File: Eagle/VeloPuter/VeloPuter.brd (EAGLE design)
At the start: 98.7 x 58.4 mm, 39 parts, among them IC1 LM2931, IC2 B7546, IC3 B7546, Q1 BSS92, Q2 BSS101

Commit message: - Added alternative components for the LDDs to be   placed at the same positions - Added 5V USB - Added overall Power off - Added 6th LDD/switch (was 5) -> possible also for buzzer.   Note that a key for this is NOT available. Possibly the   config or the hazzard button can be freed for this.
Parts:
- removed BLINKERS: (no value), con-phoenix_3.81_mcv:MCV4
- removed H1, H2, H3: MOUNT-HOLE3.6, holes:3,6
- removed IC1: LM2931, v-reg-3-gbeu:TO220L1
- added AUX_OUT: Aux, con-phoenix_3.81_mcv:MCV6
- added DC1: R-78C5.0-1.0, dc-dc-converter:SIP3
- added JP1, JP2, JP3, JP4, JP5, JP6: (no value), jumper:JP1
- added LM2931: 7805TV, linear:TO220V
- added Q10, Q12, Q14, Q4, Q6, Q8: (no value), transistor-power:TO220BV
- added Q11, Q13, Q3, Q5, Q7, Q9: BS170, transistor-small-signal:SOT54E
- added RN1: 100k, resistor-sil:SIL7
- IC2: device transistor-power:TO220BH -> transistor-small-signal:SOT54E
- IC3: device transistor-power:TO220BH -> transistor-power:TO220BV
- LIGHTS: value (none) -> Lights; device con-phoenix_3.81_mcv:MCV6 -> con-phoenix_3.81_mcv:MCV8
- Q1: value BSS92 -> (none); device transistor-fet:TO92 -> transistor-power:TO220BV
- Q2: value BSS101 -> BS170; device transistor-fet:TO92 -> transistor-small-signal:SOT54E
- moved R9 526.3 mm to (-80.0, -455.9), turned to 0 degrees
- moved R10 501.8 mm to (-80.0, -517.5)
- moved Q2 473.9 mm to (-1.27, -530.2)
- moved R4 470.6 mm to (-80.0, -394.3), turned to 0 degrees
- moved R3 403.9 mm to (-80.0, -332.7), turned to 0 degrees
- moved R2 341.0 mm to (-80.0, -271.1), turned to 0 degrees
- moved R1 274.1 mm to (-65.4, -209.6)
- moved LIGHTS 241.0 mm to (-54.6, -142.9), turned to 0 degrees
- turned IC2 to 270 degrees
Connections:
- removed net N$12: LIGHTS.3, U$5.+VOUT
- removed net ONOFF: ARDUINO_MICRO.A5, Q2.2
- new net N$17: Q3.D, Q4.G, R1.1
- new net N$23: Q7.D, Q8.G, R3.1
- new net N$28: Q10.G, Q9.D, R4.1
- new net N$29: AUX_OUT.1, Q12.S, U$5.+VOUT
- new net N$33: Q11.D, Q12.G, R9.1
- new net N$34: AUX_OUT.3, Q14.S, U$1.+VOUT
- new net N$39: AUX_OUT.4, JP6.2, U$1.-VOUT
- new net N$40: Q13.D, Q14.G, R10.1
- new net POWER_ONOFF: ARDUINO_MICRO.A5, Q2.G
- new net V_USB: AUX_OUT.5, DC1.3
- net 5V: now also CAD.3, LM2931.3; no longer CAD.1, IC1.3
- net CAD_SWITCH: now also CAD.1; no longer CAD.3
- net GND: now also AUX_OUT.6, DC1.2, JP1.1, JP2.1, JP3.1, JP4.1, JP5.1, JP6.1, LM2931.2, Q11.S, Q13.S, Q2.S, Q3.S, Q5.S, Q7.S, Q9.S, RN1.1; no longer IC1.2, Q2.1, R1.1, R10.1, R2.1, R3.1, R4.1, R9.1
- net N$10: now also Q4.S
- net N$11: now also JP1.2
- net N$13: now also AUX_OUT.2, JP5.2; no longer LIGHTS.4
- net N$15: now also Q1.G, Q2.D; no longer Q1.1, Q2.3
- net N$20: now also Q5.D, Q6.G, R2.1; no longer BRAKE.+VIN
- net N$3: now also LIGHTS.3, Q6.S; no longer LIGHTS.5
- net N$5: now also JP2.2, LIGHTS.4; no longer LIGHTS.6
- net N$6: now also LIGHTS.5, Q8.S; no longer BLINKERS.1
- net N$7: now also JP3.2, LIGHTS.6; no longer BLINKERS.2
- net N$8: now also LIGHTS.7, Q10.S; no longer BLINKERS.3
- net N$9: now also JP4.2, LIGHTS.8; no longer BLINKERS.4
- net ONOFF_AUX2: now also Q13.G, RN1.2; no longer R10.2
- net PWM_AUX1: now also Q11.G, RN1.3; no longer R9.2
- net PWM_FRONT: now also Q3.G, RN1.5; no longer R4.2
- net PWM_LEFT: now also Q7.G, RN1.7; no longer R2.2
- net PWM_REAR: now also Q5.G, RN1.4; no longer R1.2
- net PWM_RIGHT: now also Q9.G, RN1.6; no longer R3.2
- net V+: now also LM2931.1, Q1.D; no longer IC1.1, Q1.2
- net VDD: now also BRAKE.+VIN, DC1.1, Q1.S, Q10.D, Q12.D, Q14.D, Q4.D, Q6.D, Q8.D, R1.2, R10.2, R2.2, R3.2, R4.2, R9.2; no longer Q1.3
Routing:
- net PWM_RIGHT: track 102.8 -> 0.00 mm, vias 2 -> 0
- net 5V: track 93.7 -> 0.00 mm
- net PWM_LEFT: track 89.8 -> 0.00 mm
- net PWM_REAR: track 83.5 -> 0.00 mm
- net V+: track 72.2 -> 0.00 mm
- net PWM_FRONT: track 69.9 -> 0.00 mm
- net PWM_AUX1: track 67.4 -> 0.00 mm
- net N$14: track 66.7 -> 0.00 mm
- net SDA_OLED: track 51.9 -> 0.00 mm
- net V_0: track 50.7 -> 0.00 mm
- net SCL_OLED: track 48.4 -> 0.00 mm
- net CONFIG_SWITCH: track 46.8 -> 0.00 mm
- net ALARM_SWITCH: track 37.4 -> 0.00 mm
- net CAD_SWITCH: track 36.6 -> 0.00 mm
- net PWM_BUZZER: track 35.7 -> 0.00 mm
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- removed copper zone on layer 1, net GND
- removed copper zone on layer 16, net GND
- removed copper zone on layer 1, net V+
- removed copper zone on layer 1, net V-
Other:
- board size 98.7 x 58.4 mm -> 100 x 59.7 mm

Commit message: Finished placing the components. Next: routing the connections.
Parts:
- Q1, Q10, Q12, Q14, Q4, Q6, Q8: value (none) -> 4P04L04
- R7: value 3M -> 300k
- R8: value 1M -> 100k
- moved Q3 640.8 mm to (6.99, 34.3)
- moved Q5 628.3 mm to (18.4, 34.3)
- moved Q7 616.1 mm to (29.8, 34.3)
- moved Q9 604.1 mm to (41.3, 34.3)
- moved Q11 592.4 mm to (52.7, 34.3)
- moved Q13 580.9 mm to (64.1, 34.3)
- moved R10 570.3 mm to (59.1, 35.6), turned to 270 degrees
- moved Q14 549.6 mm to (60.3, 45.7), turned to 90 degrees
- moved JP6 539.9 mm to (66.7, 47.0)
- moved Q2 536.8 mm to (78.1, 0.64)
- moved R9 507.8 mm to (47.6, 35.6), turned to 270 degrees
- moved Q12 487.2 mm to (48.9, 45.7), turned to 90 degrees
- moved JP5 477.6 mm to (55.2, 47.0)
- moved R4 445.3 mm to (36.2, 35.6), turned to 270 degrees
- moved Q10 424.8 mm to (37.5, 45.7), turned to 90 degrees
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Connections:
- net V- renamed N$2
- net V+: no longer R7.2
- net VDD: now also R7.2
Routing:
- net N$17: track 0.00 -> 12.7 mm
- net PWM_FRONT: track 0.00 -> 5.71 mm
- net N$10: track 0.00 -> 4.45 mm
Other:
- board size 100 x 59.7 mm -> 101.3 x 63.5 mm

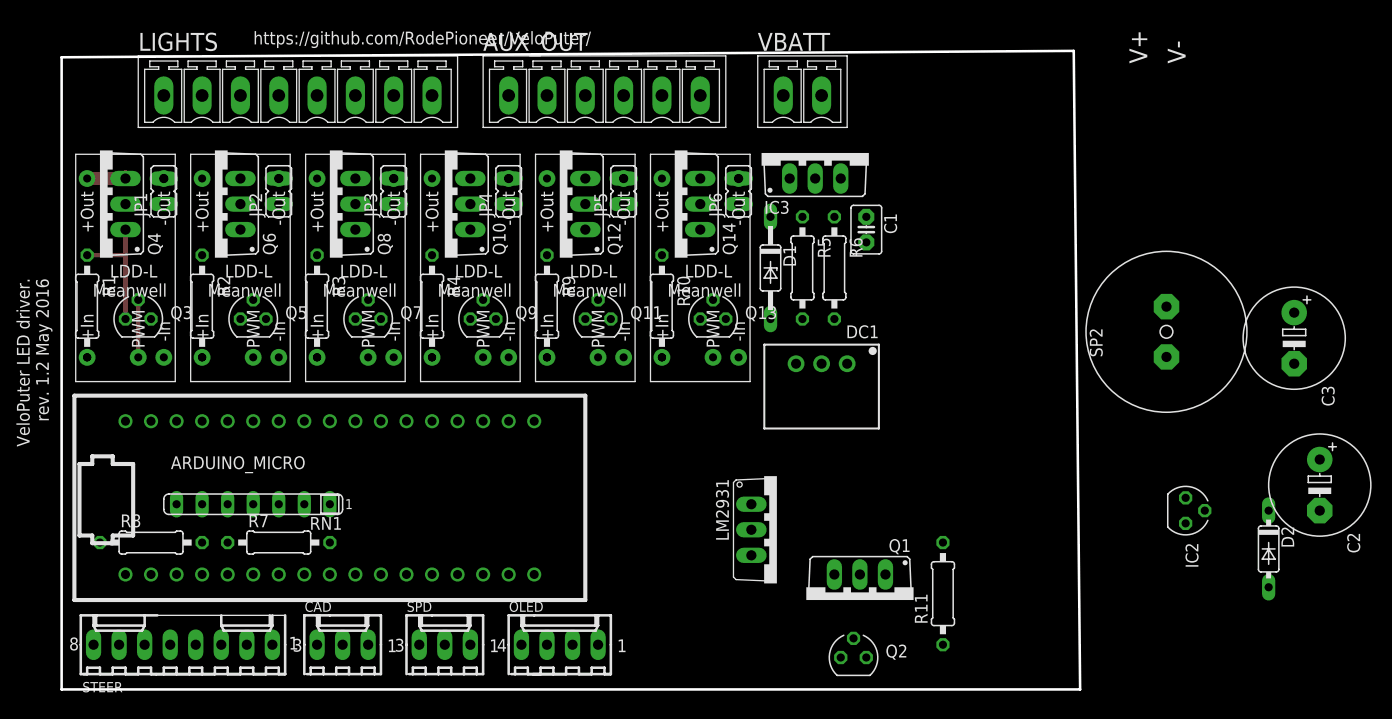
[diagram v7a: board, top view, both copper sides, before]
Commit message: Routing done. Next: tripple check everything (such as pinning, lost connections, spacings, design rules etc, etc
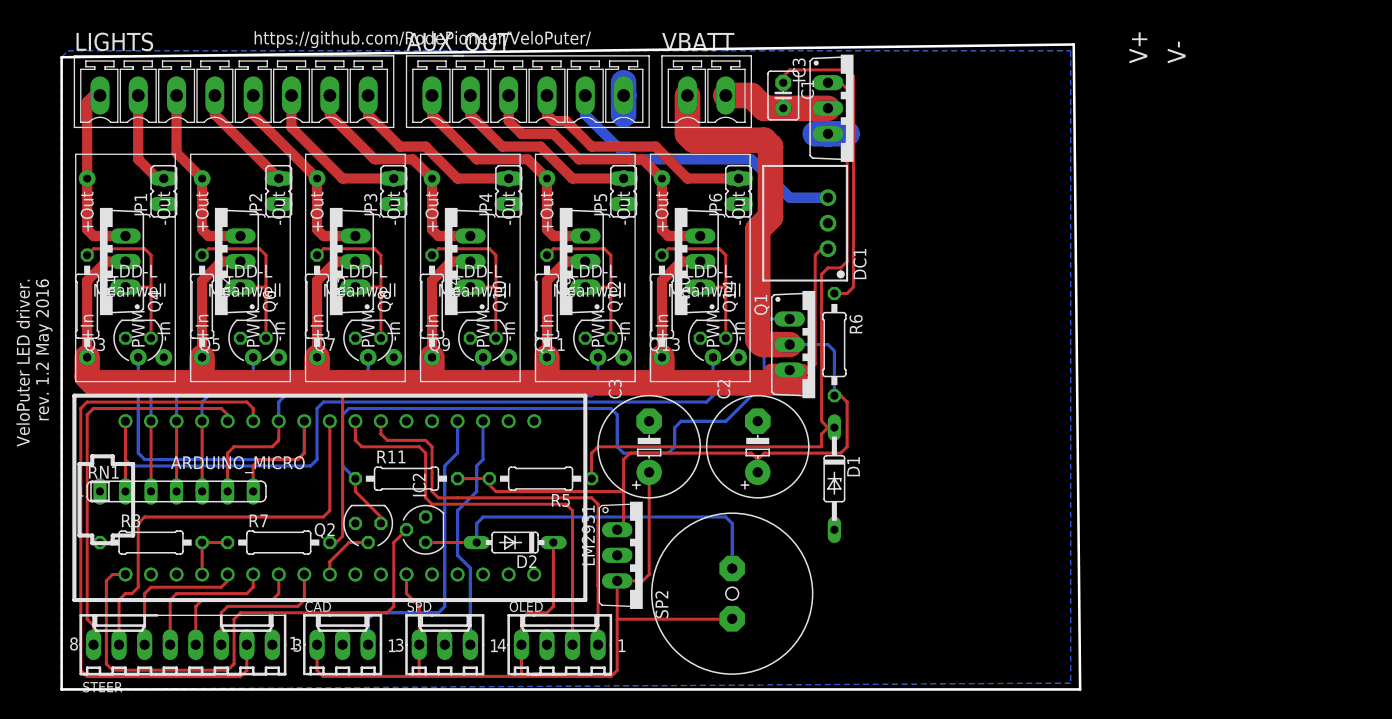
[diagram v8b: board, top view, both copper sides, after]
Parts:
- moved IC2 75.6 mm to (35.6, 13.3), turned to 90 degrees
- moved D2 74.9 mm to (44.5, 12.1), turned to 180 degrees
- moved C3 65.0 mm to (57.8, 21.6), turned to 90 degrees
- moved C2 56.0 mm to (68.6, 21.6), turned to 90 degrees
- moved R11 54.6 mm to (33.7, 18.4), turned to 0 degrees
- moved SP2 50.4 mm to (66.0, 6.99)
- moved Q2 50.1 mm to (29.8, 14.0), turned to 180 degrees
- moved R5 33.4 mm to (47.0, 18.4), turned to 180 degrees
- moved Q1 25.8 mm to (74.3, 31.8), turned to 270 degrees
- moved D1 21.9 mm to (76.2, 18.4)
- moved C1 15.7 mm to (71.1, 56.5)
- moved DC1 14.0 mm to (75.6, 43.8), turned to 90 degrees
- moved LM2931 13.6 mm to (57.1, 10.8)
- moved VBATT 9.53 mm to (63.5, 56.5)
- moved RN1 7.73 mm to (10.8, 17.1), turned to 0 degrees
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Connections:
- net N$10 renamed FRONT+
- net N$11 renamed FRONT-
- net N$13 renamed AUX1-
- net N$2 renamed V-
- net N$29 renamed AUX1+
- net N$3 renamed REAR+
- net N$34 renamed AUX2+
- net N$39 renamed AUX2-
- net N$5 renamed REAR-
- net N$6 renamed LEFT+
- net N$7 renamed LEFT-
- net N$8 renamed RIGHT+
- net N$9 renamed RIGHT-
- net PWM_AUX1: now also RN1.6; no longer RN1.3
- net PWM_FRONT: now also RN1.7; no longer RN1.5
- net PWM_LEFT: now also RN1.4; no longer RN1.7
- net PWM_REAR: now also RN1.3; no longer RN1.4
- net PWM_RIGHT: now also RN1.5; no longer RN1.6
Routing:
- net VDD: track 0.00 -> 193.7 mm
- net V+: track 0.00 -> 100.9 mm
- net 5V: track 0.00 -> 93.2 mm
- net ONOFF_AUX2: track 0.00 -> 79.2 mm
- net N$15: track 0.00 -> 70.8 mm
- net N$4: track 0.00 -> 66.4 mm
- net BRAKE_SWITCH: track 0.00 -> 64.6 mm
- net PWM_BUZZER: track 0.00 -> 52.6 mm
- net PWM_AUX1: track 0.00 -> 48.7 mm
- net SDA_OLED: track 0.00 -> 42.3 mm
- net SCL_OLED: track 0.00 -> 42.3 mm
- net CONFIG_SWITCH: track 0.00 -> 41.7 mm
- net PWM_RIGHT: track 0.00 -> 39.8 mm
- net ALARM_SWITCH: track 0.00 -> 38.3 mm
- net N$14: track 0.00 -> 37.4 mm
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- added copper zone on layer 16, net GND
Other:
- board size 101.3 x 63.5 mm -> 101.3 x 64.1 mm
